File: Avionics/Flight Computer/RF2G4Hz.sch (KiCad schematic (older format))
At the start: 34 parts, among them J2 CONN_COAXIAL, U3 CC2650F128RGZR, U4 CC2592RGVR

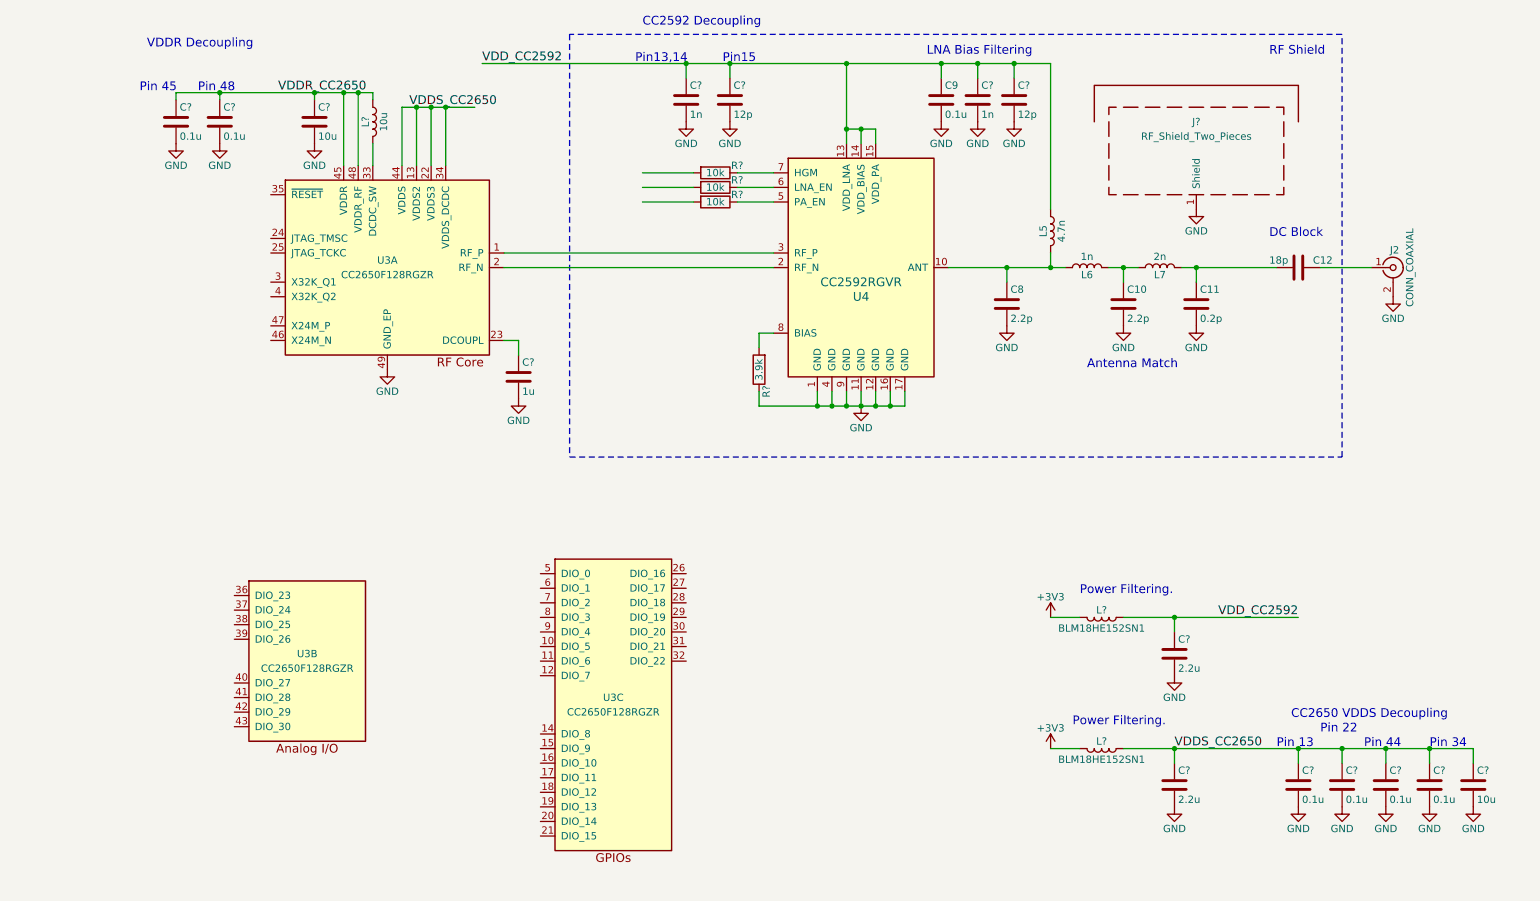
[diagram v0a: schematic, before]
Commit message: Added more RF passives and placement of RF front ends
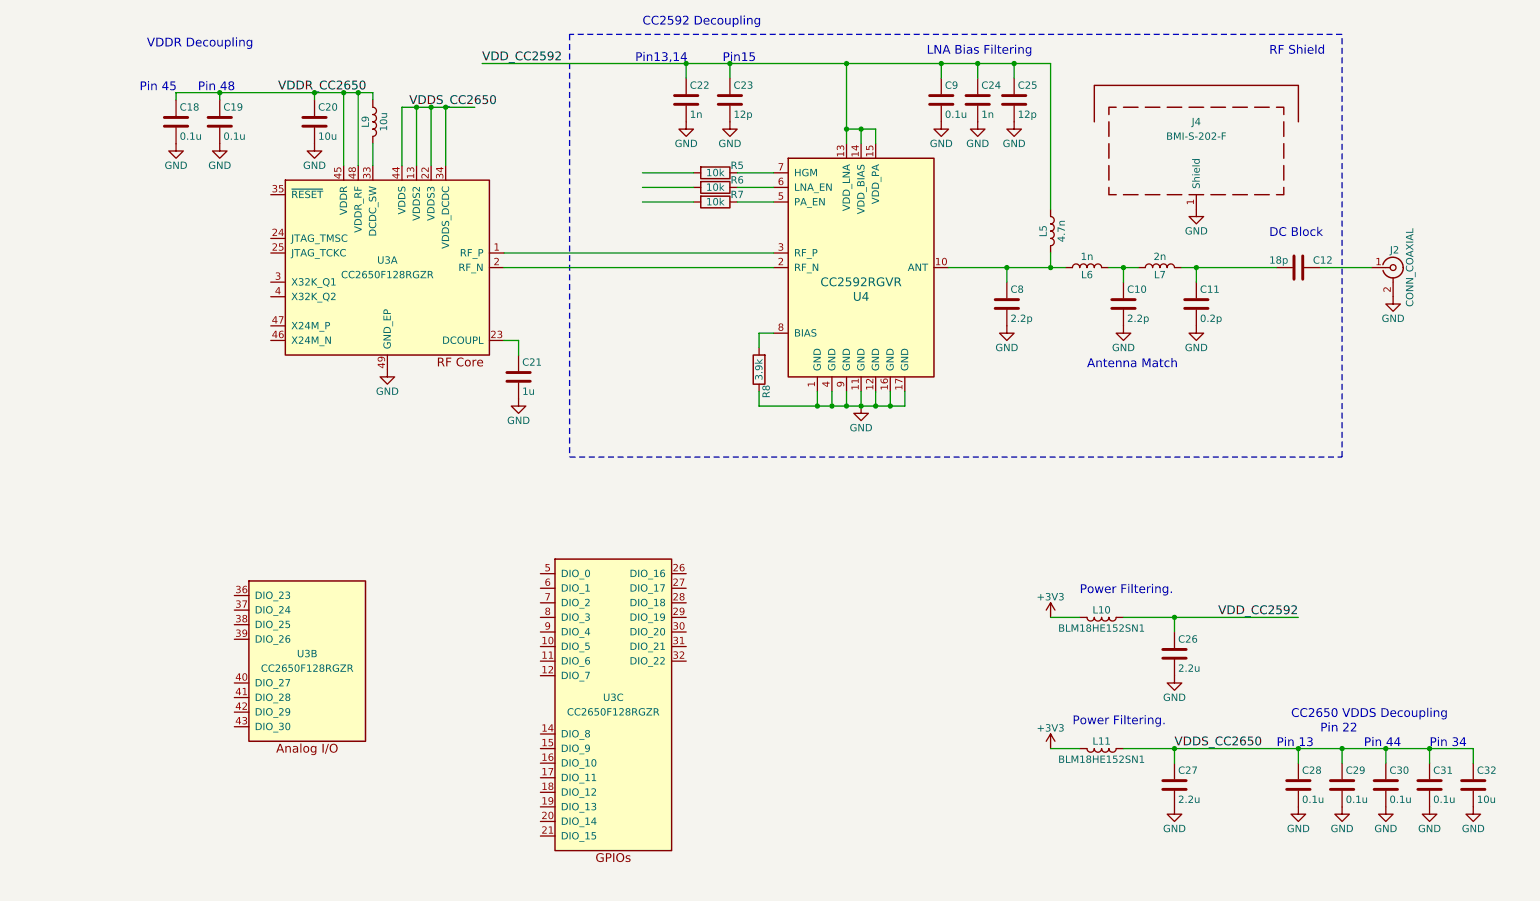
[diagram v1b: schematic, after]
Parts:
- C26, C27: renamed from C?; footprint Inductors_SMD:L_0805 -> Capacitors_SMD:C_0603
- J4: renamed from J?; value RF_Shield_Two_Pieces -> BMI-S-202-F; footprint (none) -> Shielding_Cabinets:Laird_Technologies_BMI-S-202-F_16.50x16.50mm
- R5, R6, R7, R8: renamed from R?; footprint (none) -> Resistors_SMD:R_0402
- gave numbers to parts that had none: 16

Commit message: Lots of power tree and layout work
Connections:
- net labels added: +3.3V
- net labels removed: +3V3
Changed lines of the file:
@@
 LIBS:graphic
 LIBS:power
+LIBS:interface
+LIBS:linear
+LIBS:74xgxx
+LIBS:74xx
+LIBS:ac-dc
+LIBS:actel
+LIBS:adc-dac
+LIBS:allegro
+LIBS:Altera
+LIBS:analog_devices
+LIBS:analog_switches
+LIBS:Power_Management
+LIBS:powerint
 LIBS:Flight Computer-cache
-EELAYER 25 0
+EELAYER 26 0
 EELAYER END
 $Descr A4 11693 8268
@@
 $EndComp
 $Comp
-L GND #PWR41
+L GND #PWR031
 U 1 1 58AA6B6F
 P 7100 2700
-F 0 "#PWR41" H 7100 2450 50  0001 C CNN
+F 0 "#PWR031" H 7100 2450 50  0001 C CNN
 F 1 "GND" H 7100 2550 50  0000 C CNN
 F 2 "" H 7100 2700 50  0001 C CNN
@@
 $EndComp
 $Comp
-L GND #PWR45
+L GND #PWR032
 U 1 1 58AA6B99
 P 7900 2700
-F 0 "#PWR45" H 7900 2450 50  0001 C CNN
+F 0 "#PWR032" H 7900 2450 50  0001 C CNN
 F 1 "GND" H 7900 2550 50  0000 C CNN
 F 2 "" H 7900 2700 50  0001 C CNN
@@
 $EndComp
 $Comp
-L GND #PWR49
+L GND #PWR033
 U 1 1 58AA6BBC
 P 8400 2700
-F 0 "#PWR49" H 8400 2450 50  0001 C CNN
+F 0 "#PWR033" H 8400 2450 50  0001 C CNN
 F 1 "GND" H 8400 2550 50  0000 C CNN
 F 2 "" H 8400 2700 50  0001 C CNN
@@
 $EndComp
 $Comp
-L GND #PWR39
+L GND #PWR034
 U 1 1 58AA6BDF
 P 6650 1300
-F 0 "#PWR39" H 6650 1050 50  0001 C CNN
+F 0 "#PWR034" H 6650 1050 50  0001 C CNN
 F 1 "GND" H 6650 1150 50  0000 C CNN
 F 2 "" H 6650 1300 50  0001 C CNN
@@
 $EndComp
 $Comp
-L GND #PWR53
+L GND #PWR035
 U 1 1 58AA6E83
 P 9750 2500
-F 0 "#PWR53" H 9750 2250 50  0001 C CNN
+F 0 "#PWR035" H 9750 2250 50  0001 C CNN
 F 1 "GND" H 9750 2350 50  0000 C CNN
 F 2 "" H 9750 2500 50  0001 C CNN
@@
 $EndComp
 $Comp
-L GND #PWR48
+L GND #PWR036
 U 1 1 58AB3920
 P 8400 1900
-F 0 "#PWR48" H 8400 1650 50  0001 C CNN
+F 0 "#PWR036" H 8400 1650 50  0001 C CNN
 F 1 "GND" H 8400 1750 50  0000 C CNN
 F 2 "" H 8400 1900 50  0001 C CNN
@@
 Connection ~ 7150 900
 $Comp
-L GND #PWR40
+L GND #PWR037
 U 1 1 58AB48CB
 P 6900 1300
-F 0 "#PWR40" H 6900 1050 50  0001 C CNN
+F 0 "#PWR037" H 6900 1050 50  0001 C CNN
 F 1 "GND" H 6900 1150 50  0000 C CNN
 F 2 "" H 6900 1300 50  0001 C CNN
@@
 $EndComp
 $Comp
-L GND #PWR42
+L GND #PWR038
 U 1 1 58AB4906
 P 7150 1300
-F 0 "#PWR42" H 7150 1050 50  0001 C CNN
+F 0 "#PWR038" H 7150 1050 50  0001 C CNN
 F 1 "GND" H 7150 1150 50  0000 C CNN
 F 2 "" H 7150 1300 50  0001 C CNN
@@
 Connection ~ 8250 4700
 $Comp
-L GND #PWR46
+L GND #PWR039
 U 1 1 58AB5954
 P 8250 5100
-F 0 "#PWR46" H 8250 4850 50  0001 C CNN
+F 0 "#PWR039" H 8250 4850 50  0001 C CNN
 F 1 "GND" H 8250 4950 50  0000 C CNN
 F 2 "" H 8250 5100 50  0001 C CNN
@@
 $EndComp
 $Comp
-L GND #PWR36
+L GND #PWR040
 U 1 1 58AB599B
 P 4900 1300
-F 0 "#PWR36" H 4900 1050 50  0001 C CNN
+F 0 "#PWR040" H 4900 1050 50  0001 C CNN
 F 1 "GND" H 4900 1150 50  0000 C CNN
 F 2 "" H 4900 1300 50  0001 C CNN
@@
 $EndComp
 $Comp
-L GND #PWR37
+L GND #PWR041
 U 1 1 58AB59E2
 P 5200 1300
-F 0 "#PWR37" H 5200 1050 50  0001 C CNN
+F 0 "#PWR041" H 5200 1050 50  0001 C CNN
 F 1 "GND" H 5200 1150 50  0000 C CNN
 F 2 "" H 5200 1300 50  0001 C CNN
@@
 Wire Wire Line
 	7400 4700 7600 4700
-$Comp
-L +3V3 #PWR43
-U 1 1 58AB9101
-P 7400 4700
-F 0 "#PWR43" H 7400 4550 50  0001 C CNN
-F 1 "+3V3" H 7400 4840 50  0000 C CNN
-F 2 "" H 7400 4700 50  0001 C CNN
-F 3 "" H 7400 4700 50  0001 C CNN
-	1    7400 4700
-	1    0    0    -1
-$EndComp
 Wire Wire Line
 	7900 5600 10300 5600
@@
 	7400 5600 7600 5600
 $Comp
-L +3V3 #PWR44
-U 1 1 58AB9545
-P 7400 5600
-F 0 "#PWR44" H 7400 5450 50  0001 C CNN
-F 1 "+3V3" H 7400 5740 50  0000 C CNN
-F 2 "" H 7400 5600 50  0001 C CNN
-F 3 "" H 7400 5600 50  0001 C CNN
-	1    7400 5600
-	1    0    0    -1
-$EndComp
-$Comp
-L GND #PWR38
+L GND #PWR042
 U 1 1 58ABB30E
 P 6100 3250
-F 0 "#PWR38" H 6100 3000 50  0001 C CNN
+F 0 "#PWR042" H 6100 3000 50  0001 C CNN
 F 1 "GND" H 6100 3100 50  0000 C CNN
 F 2 "" H 6100 3250 50  0001 C CNN
@@
 Connection ~ 6300 3250
 $Comp
-L GND #PWR34
+L GND #PWR043
 U 1 1 58ABBA52
 P 2850 3000
-F 0 "#PWR34" H 2850 2750 50  0001 C CNN
+F 0 "#PWR043" H 2850 2750 50  0001 C CNN
 F 1 "GND" H 2850 2850 50  0000 C CNN
 F 2 "" H 2850 3000 50  0001 C CNN
@@
 Connection ~ 2550 1100
 $Comp
-L GND #PWR33
+L GND #PWR044
 U 1 1 58ABE732
 P 2350 1450
-F 0 "#PWR33" H 2350 1200 50  0001 C CNN
+F 0 "#PWR044" H 2350 1200 50  0001 C CNN
 F 1 "GND" H 2350 1300 50  0000 C CNN
 F 2 "" H 2350 1450 50  0001 C CNN
@@
 Connection ~ 10000 5600
 $Comp
-L GND #PWR50
+L GND #PWR045
 U 1 1 58AC3449
 P 9100 6000
-F 0 "#PWR50" H 9100 5750 50  0001 C CNN
+F 0 "#PWR045" H 9100 5750 50  0001 C CNN
 F 1 "GND" H 9100 5850 50  0000 C CNN
 F 2 "" H 9100 6000 50  0001 C CNN
@@
 $EndComp
 $Comp
-L GND #PWR51
+L GND #PWR046
 U 1 1 58AC3569
 P 9400 6000
-F 0 "#PWR51" H 9400 5750 50  0001 C CNN
+F 0 "#PWR046" H 9400 5750 50  0001 C CNN
 F 1 "GND" H 9400 5850 50  0000 C CNN
 F 2 "" H 9400 6000 50  0001 C CNN
@@
 $EndComp
 $Comp
-L GND #PWR52
+L GND #PWR047
 U 1 1 58AC35CB
 P 9700 6000
-F 0 "#PWR52" H 9700 5750 50  0001 C CNN
+F 0 "#PWR047" H 9700 5750 50  0001 C CNN
 F 1 "GND" H 9700 5850 50  0000 C CNN
 F 2 "" H 9700 6000 50  0001 C CNN
@@
 $EndComp
 $Comp
-L GND #PWR54
+L GND #PWR048
 U 1 1 58AC362D
 P 10000 6000
-F 0 "#PWR54" H 10000 5750 50  0001 C CNN
+F 0 "#PWR048" H 10000 5750 50  0001 C CNN
 F 1 "GND" H 10000 5850 50  0000 C CNN
 F 2 "" H 10000 6000 50  0001 C CNN
@@
 $EndComp
 $Comp
-L GND #PWR55
+L GND #PWR049
 U 1 1 58AC368F
 P 10300 6000
-F 0 "#PWR55" H 10300 5750 50  0001 C CNN
+F 0 "#PWR049" H 10300 5750 50  0001 C CNN
 F 1 "GND" H 10300 5850 50  0000 C CNN
 F 2 "" H 10300 6000 50  0001 C CNN
@@
 $EndComp
 $Comp
-L GND #PWR31
+L GND #PWR050
 U 1 1 58AC8629
 P 1400 1450
-F 0 "#PWR31" H 1400 1200 50  0001 C CNN
+F 0 "#PWR050" H 1400 1200 50  0001 C CNN
 F 1 "GND" H 1400 1300 50  0000 C CNN
 F 2 "" H 1400 1450 50  0001 C CNN
@@
 $EndComp
 $Comp
-L GND #PWR32
+L GND #PWR051
 U 1 1 58AC8691
 P 1700 1450
-F 0 "#PWR32" H 1700 1200 50  0001 C CNN
+F 0 "#PWR051" H 1700 1200 50  0001 C CNN
 F 1 "GND" H 1700 1300 50  0000 C CNN
 F 2 "" H 1700 1450 50  0001 C CNN
@@
 	3750 2800 3750 2900
 $Comp
-L GND #PWR35
+L GND #PWR052
 U 1 1 58ACE800
 P 3750 3200
-F 0 "#PWR35" H 3750 2950 50  0001 C CNN
+F 0 "#PWR052" H 3750 2950 50  0001 C CNN
 F 1 "GND" H 3750 3050 50  0000 C CNN
 F 2 "" H 3750 3200 50  0001 C CNN
@@
 Connection ~ 8250 5600
 $Comp
-L GND #PWR47
+L GND #PWR053
 U 1 1 58AD6FCF
 P 8250 6000
-F 0 "#PWR47" H 8250 5750 50  0001 C CNN
+F 0 "#PWR053" H 8250 5750 50  0001 C CNN
 F 1 "GND" H 8250 5850 50  0000 C CNN
 F 2 "" H 8250 6000 50  0001 C CNN
@@
 Text Notes 5150 900  0    60   ~ 0
 Pin15
+$Comp
+L +3.3V #PWR054
+U 1 1 58ABAEB2
+P 7400 4700
+F 0 "#PWR054" H 7450 4750 50  0001 C CNN
+F 1 "+3.3V" H 7415 4873 50  0000 C CNN
+F 2 "" H 50  -100 50  0001 C CNN
+F 3 "" H 50  -100 50  0001 C CNN
+	1    7400 4700
+	1    0    0    -1
+$EndComp
+$Comp
+L +3.3V #PWR055
+U 1 1 58ABAF0C
+P 7400 5600
+F 0 "#PWR055" H 7450 5650 50  0001 C CNN
+F 1 "+3.3V" H 7415 5773 50  0000 C CNN
+F 2 "" H 50  800 50  0001 C CNN
+F 3 "" H 50  800 50  0001 C CNN
+	1    7400 5600
+	1    0    0    -1
+$EndComp
 $EndSCHEMATC

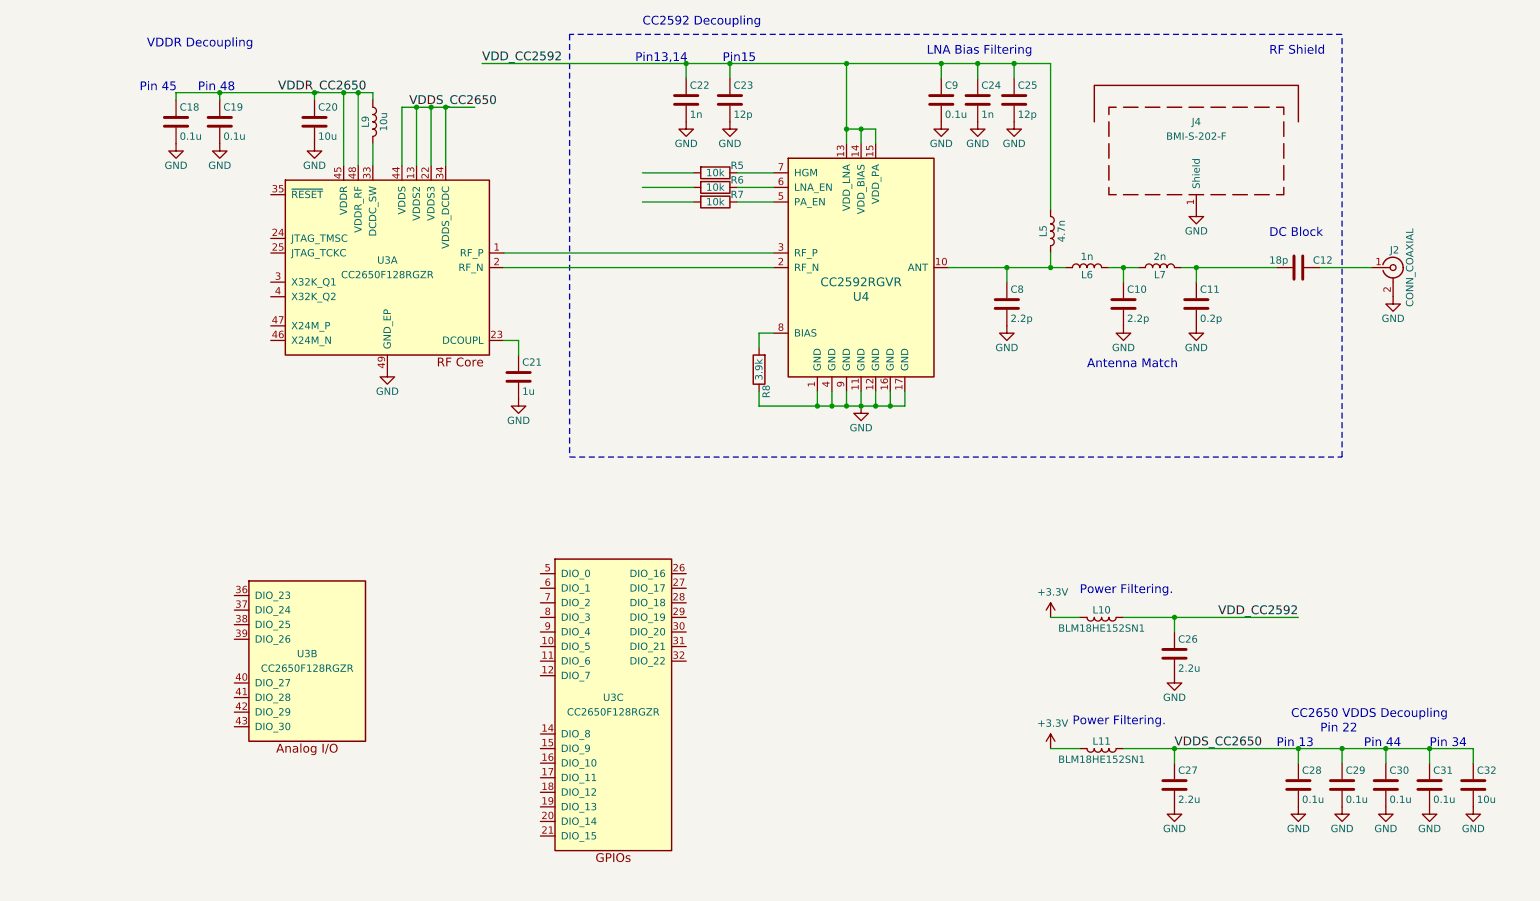
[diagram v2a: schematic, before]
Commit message: Restarted initial layout and cleaned up decoupling/RF layout.
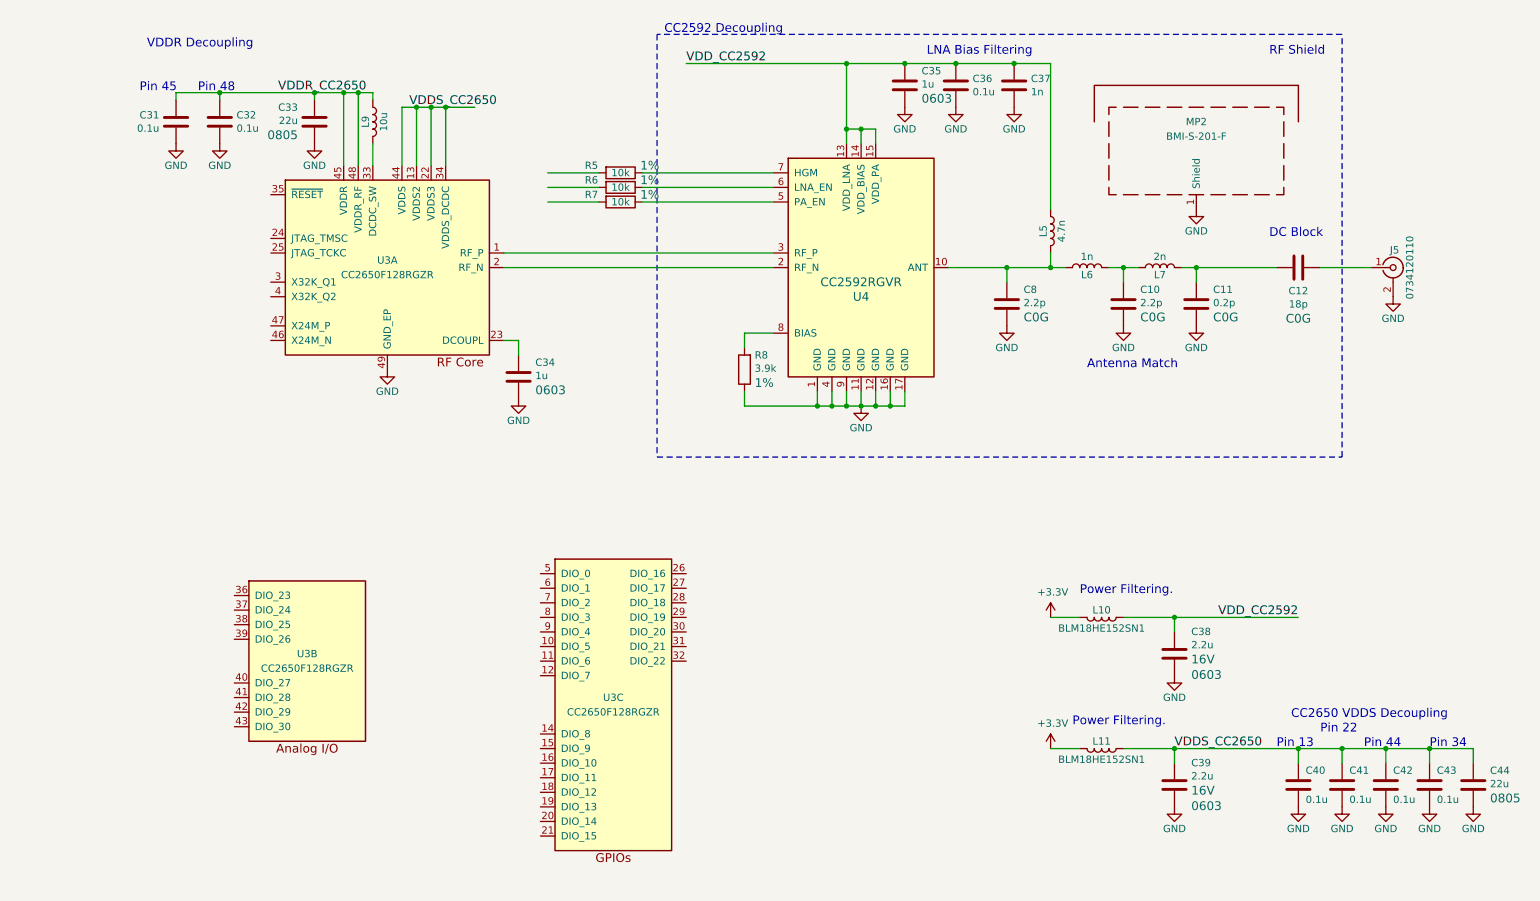
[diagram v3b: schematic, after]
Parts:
- removed C18, C19, C28, C29, C30, C9: 0.1u, Capacitors_SMD:C_0402, symbol C
- removed C20: 10u, Capacitors_SMD:C_0603, symbol C
- removed C21: 1u, Capacitors_SMD:C_0402, symbol C
- removed C22, C24: 1n, Capacitors_SMD:C_0402, symbol C
- removed C23, C25: 12p, Capacitors_SMD:C_0402, symbol C
- removed C26, C27: 2.2u, Capacitors_SMD:C_0603, symbol C
- added C33, C44: 22u, Capacitors_SMD:C_0805, symbol C
- added C34, C35: 1u, Capacitors_SMD:C_0603, symbol C
- added C36, C40, C41, C42, C43: 0.1u, Capacitors_SMD:C_0402, symbol C
- added C37: 1n, Capacitors_SMD:C_0402, symbol C
- added C38, C39: 2.2u, Capacitors_SMD:C_0603, symbol C
- C10, C11, C12, C8: Package (none) -> 0402; Tolerance (none) -> 20%; Type (none) -> C0G; Voltage (none) -> 50V
- C31: Package (none) -> 0402; Tolerance (none) -> 20%; Type (none) -> X7R; Voltage (none) -> 50V
- C32: value 10u -> 0.1u; footprint Capacitors_SMD:C_0603 -> Capacitors_SMD:C_0402; Package (none) -> 0402; Tolerance (none) -> 20%; Type (none) -> X7R; Voltage (none) -> 50V
- J5: renamed from J2; value CONN_COAXIAL -> 0734120110
- L5: Package (none) -> 0402
- MP2: renamed from J4; value BMI-S-202-F -> BMI-S-201-F; footprint Shielding_Cabinets:Laird_Technologies_BMI-S-202-F_16.50x16.50mm -> Shielding_Cabinets:Laird_Technologies_BMI-S-201-F_13.66x12.70mm
- R5, R6, R7, R8: Material (none) -> Thin Film; Package (none) -> 0402; Power (none) -> 0.062W; Tolerance (none) -> 1%; Voltage (none) -> 50V
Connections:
- wire segments 64 -> 88
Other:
- note removed: "Pin13,14"
- note removed: "Pin15"

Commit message: Nearly completed initial placement.
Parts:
- added C70, C71: 12p, Capacitors_SMD:C_0402, symbol C
- added Y5: XRCGB24M000F2P00R0, Crystals:Crystal_SMD_2016-4pin_2.0x1.6mm, symbol Crystal_GND24
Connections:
- net labels added: ADIO-23, ADIO-24, ADIO-25, ADIO-26, ADIO-27, ADIO-28, ADIO-29, ADIO-30, ADIO-[23..30], RF50_2.4_1, RF50_2.4_2, RF50_2.4_3, RF50_2.4_ANT, RF50_2.4_N, RF50_2.4_P, SSI0-CLK, SSI0-FSS, SSI0-RX, SSI0-TX, UART0-RX, UART0-TX
- wire segments 88 -> 82
- no-connect marks 0 -> 4
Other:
- note added: "Using BLE without RTC Crystal requires calibration over temp:\nhttp://www.ti.com/lit/an/swra499a/swra499a.pdf"
- moved on the sheet: C39, C44, MP2, U3B, U3C
